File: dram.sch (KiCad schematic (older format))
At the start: 25 parts

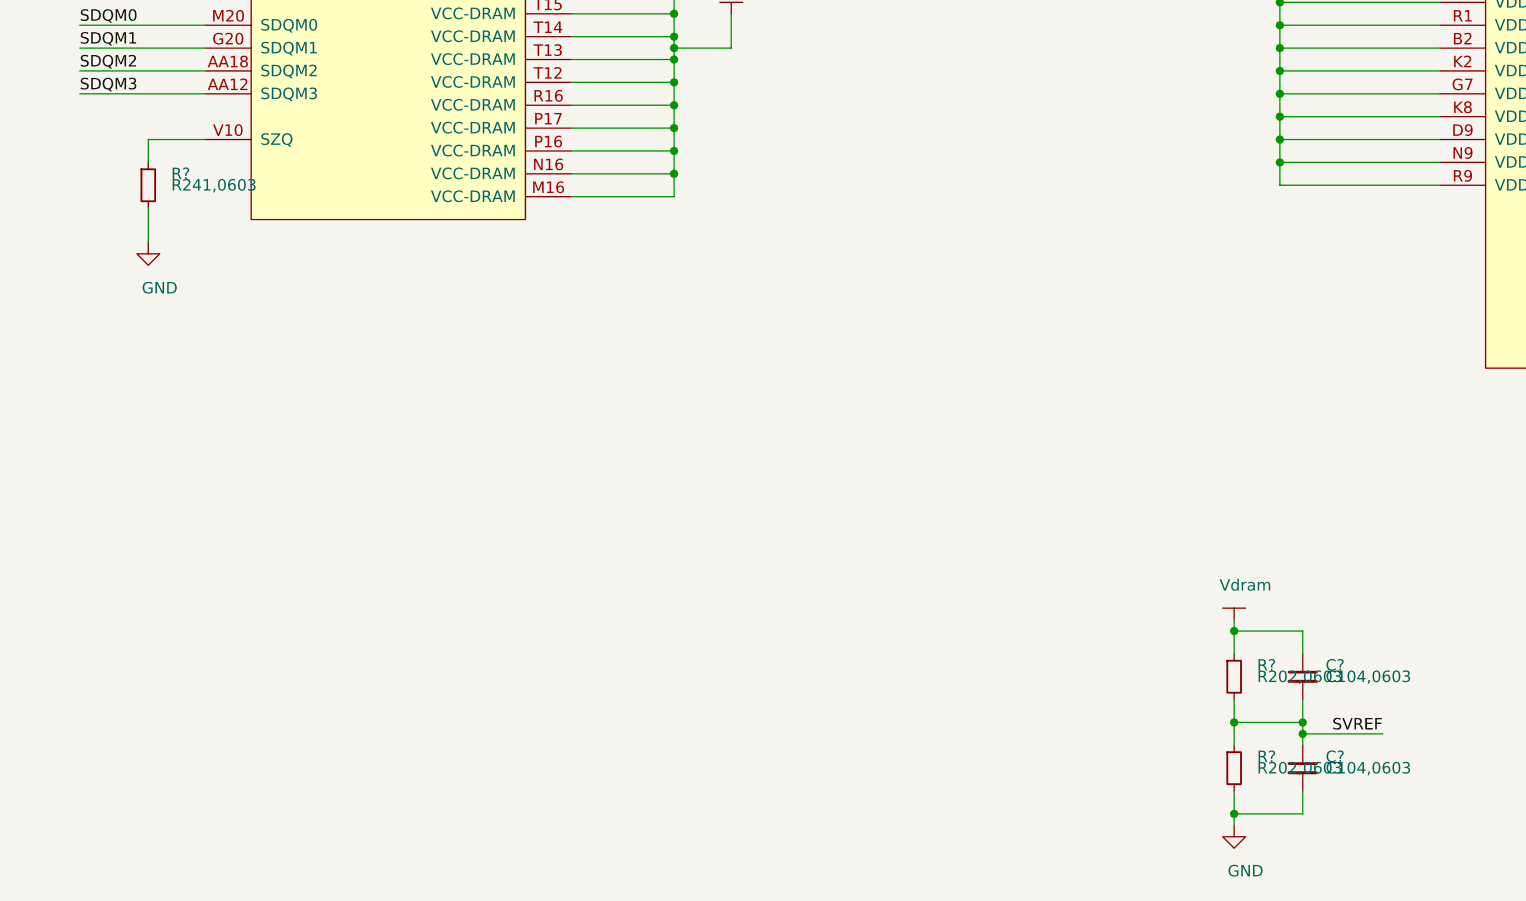
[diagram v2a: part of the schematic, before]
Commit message: update Vdram capacitor,
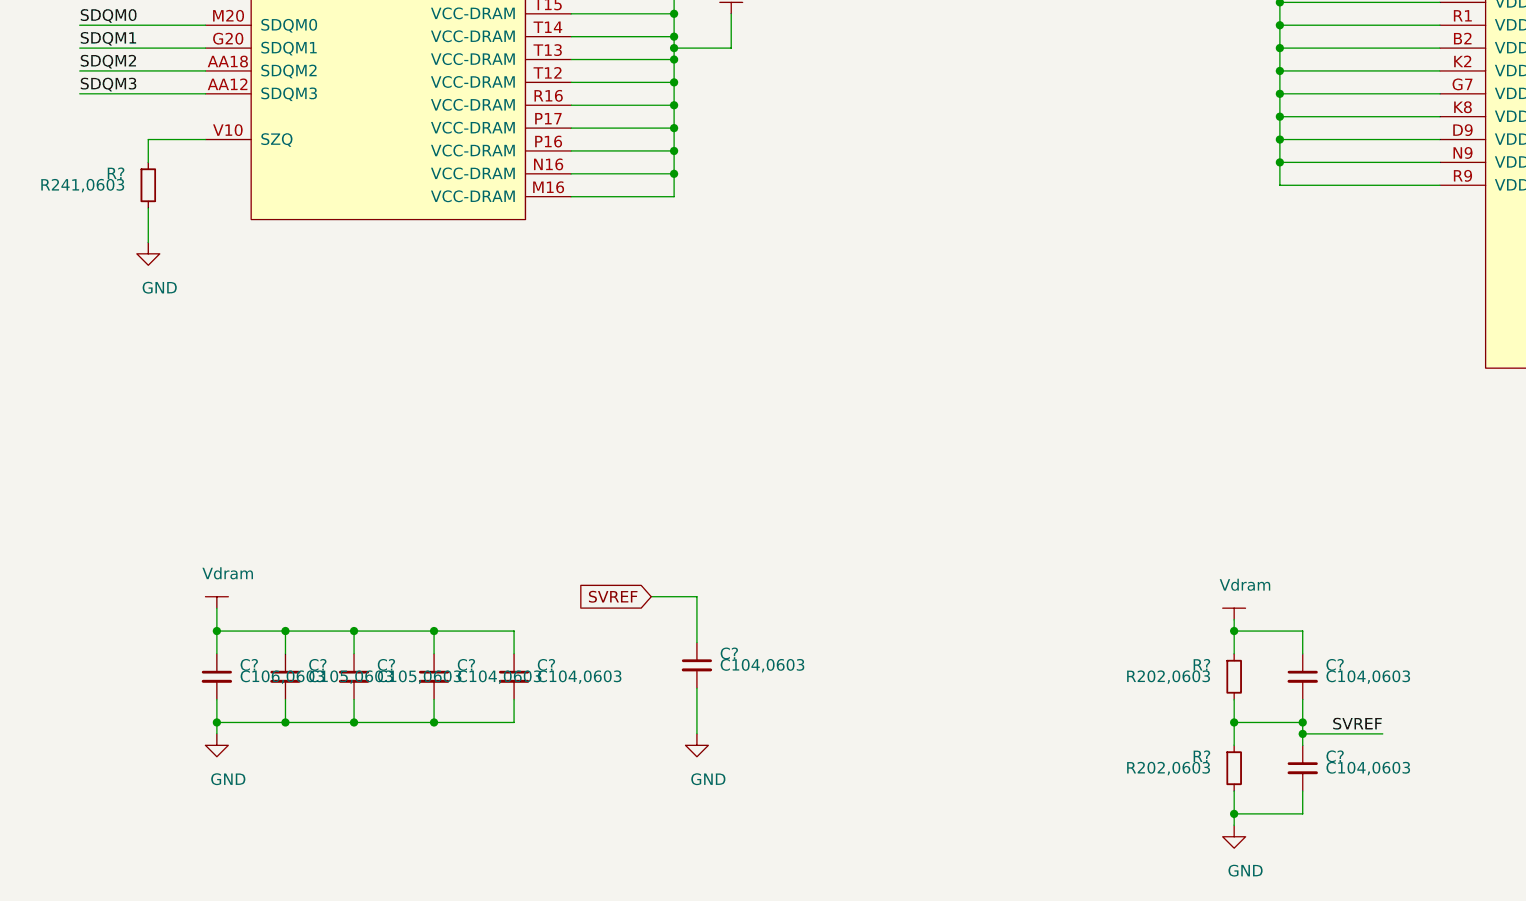
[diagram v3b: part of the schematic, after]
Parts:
- added C?: C106,0603, Capacitor_SMD:C_0603_1608Metric_Pad1.05x0.95mm_HandSolder, symbol taobao-c:C106,0603
- added C? (x2): C105,0603, Capacitor_SMD:C_0603_1608Metric_Pad1.05x0.95mm_HandSolder, symbol taobao-c:C105,0603
- added C? (x3): C104,0603, Capacitor_SMD:C_0603_1608Metric_Pad1.05x0.95mm_HandSolder, symbol taobao-c:C104,0603
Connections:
- net GND: now also C?.2, C?.2, C?.2, C?.2, C?.2, C?.2
- net SVREF: now also C?.1
- net Vdram: now also C?.1, C?.1, C?.1, C?.1, C?.1
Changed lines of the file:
@@
 AR Path="/5C5C55F2/5C2CA6EE" Ref="R?"  Part="1"
 AR Path="/5C273FE9/5C2CA6EE" Ref="R?"  Part="1"
-F 0 "R?" H 6950 9050 50  0000 L CNN
-F 1 "R202,0603" H 6950 9000 50  0000 L CNN
+F 0 "R?" H 6750 9050 50  0000 R CNN
+F 1 "R202,0603" H 6750 9000 50  0000 R CNN
 F 2 "Resistor_SMD:R_0603_1608Metric_Pad1.05x0.95mm_HandSolder" H 6850 9000 50  0001 C CNN
 F 3 "~" H 6850 9000 50  0001 C CNN
@@
 AR Path="/5C5C55F2/5C2CA73C" Ref="R?"  Part="1"
 AR Path="/5C273FE9/5C2CA73C" Ref="R?"  Part="1"
-F 0 "R?" H 6950 9450 50  0000 L CNN
-F 1 "R202,0603" H 6950 9400 50  0000 L CNN
+F 0 "R?" H 6750 9450 50  0000 R CNN
+F 1 "R202,0603" H 6750 9400 50  0000 R CNN
 F 2 "Resistor_SMD:R_0603_1608Metric_Pad1.05x0.95mm_HandSolder" H 6850 9400 50  0001 C CNN
 F 3 "~" H 6850 9400 50  0001 C CNN
@@
 U 1 1 5C5FA017
 P 2100 6850
-F 0 "R?" H 2200 6900 50  0000 L CNN
-F 1 "R241,0603" H 2200 6850 50  0000 L CNN
+F 0 "R?" H 2000 6900 50  0000 R CNN
+F 1 "R241,0603" H 2000 6850 50  0000 R CNN
 F 2 "Resistor_SMD:R_0603_1608Metric_Pad1.05x0.95mm_HandSolder" H 2100 6850 50  0001 C CNN
 F 3 "~" H 2100 6850 50  0001 C CNN
@@
 Wire Wire Line
 	1850 5050 2350 5050
+$Comp
+L taobao-components:Vdram #PWR?
+U 1 1 5C2AD72D
+P 2400 8700
+AR Path="/5C273FE9/5C786D7F/5C2AD72D" Ref="#PWR?"  Part="1"
+AR Path="/5C273FE9/5C7AC496/5C2AD72D" Ref="#PWR?"  Part="1"
+AR Path="/5C7B767A/5C786D7F/5C2AD72D" Ref="#PWR?"  Part="1"
+F 0 "#PWR?" H 2400 8550 50  0001 C CNN
+F 1 "Vdram" H 2450 8850 50  0000 C CNN
+F 2 "" H 2400 8700 50  0001 C CNN
+F 3 "" H 2400 8700 50  0001 C CNN
+	1    2400 8700
+	1    0    0    -1
+$EndComp
+$Comp
+L taobao-c:C106,0603 C?
+U 1 1 5C2AD733
+P 2400 9000
+AR Path="/5C273FE9/5C786D7F/5C2AD733" Ref="C?"  Part="1"
+AR Path="/5C273FE9/5C7AC496/5C2AD733" Ref="C?"  Part="1"
+AR Path="/5C7B767A/5C786D7F/5C2AD733" Ref="C?"  Part="1"
+F 0 "C?" H 2500 9050 50  0000 L CNN
+F 1 "C106,0603" H 2500 9000 50  0000 L CNN
+F 2 "Capacitor_SMD:C_0603_1608Metric_Pad1.05x0.95mm_HandSolder" H 2400 9000 50  0001 C CNN
+F 3 "~" H 2400 9000 50  0001 C CNN
+	1    2400 9000
+	1    0    0    -1
+$EndComp
+$Comp
+L power:GND #PWR?
+U 1 1 5C2AD73A
+P 2400 9250
+AR Path="/5C273FE9/5C786D7F/5C2AD73A" Ref="#PWR?"  Part="1"
+AR Path="/5C273FE9/5C7AC496/5C2AD73A" Ref="#PWR?"  Part="1"
+AR Path="/5C7B767A/5C786D7F/5C2AD73A" Ref="#PWR?"  Part="1"
+F 0 "#PWR?" H 2400 9000 50  0001 C CNN
+F 1 "GND" H 2450 9050 50  0000 C CNN
+F 2 "" H 2400 9250 50  0001 C CNN
+F 3 "" H 2400 9250 50  0001 C CNN
+	1    2400 9250
+	1    0    0    -1
+$EndComp
+Wire Wire Line
+	2400 9250 2400 9200
+Wire Wire Line
+	2400 8700 2400 8800
+$Comp
+L taobao-c:C105,0603 C?
+U 1 1 5C2AD742
+P 2700 9000
+AR Path="/5C273FE9/5C786D7F/5C2AD742" Ref="C?"  Part="1"
+AR Path="/5C273FE9/5C7AC496/5C2AD742" Ref="C?"  Part="1"
+AR Path="/5C7B767A/5C786D7F/5C2AD742" Ref="C?"  Part="1"
+F 0 "C?" H 2800 9050 50  0000 L CNN
+F 1 "C105,0603" H 2800 9000 50  0000 L CNN
+F 2 "Capacitor_SMD:C_0603_1608Metric_Pad1.05x0.95mm_HandSolder" H 2700 9000 50  0001 C CNN
+F 3 "~" H 2700 9000 50  0001 C CNN
+	1    2700 9000
+	1    0    0    -1
+$EndComp
+Wire Wire Line
+	2700 8900 2700 8800
+Wire Wire Line
+	2700 8800 2400 8800
+Connection ~ 2400 8800
+Wire Wire Line
+	2400 8800 2400 8900
+Wire Wire Line
+	2700 9100 2700 9200
+Wire Wire Line
+	2700 9200 2400 9200
+Connection ~ 2400 9200
+Wire Wire Line
+	2400 9200 2400 9100
+$Comp
+L taobao-c:C105,0603 C?
+U 1 1 5C2AD751
+P 3000 9000
+AR Path="/5C273FE9/5C786D7F/5C2AD751" Ref="C?"  Part="1"
+AR Path="/5C273FE9/5C7AC496/5C2AD751" Ref="C?"  Part="1"
+AR Path="/5C7B767A/5C786D7F/5C2AD751" Ref="C?"  Part="1"
+F 0 "C?" H 3100 9050 50  0000 L CNN
+F 1 "C105,0603" H 3100 9000 50  0000 L CNN
+F 2 "Capacitor_SMD:C_0603_1608Metric_Pad1.05x0.95mm_HandSolder" H 3000 9000 50  0001 C CNN
+F 3 "~" H 3000 9000 50  0001 C CNN
+	1    3000 9000
+	1    0    0    -1
+$EndComp
+Wire Wire Line
+	3000 8900 3000 8800
+Wire Wire Line
+	3000 8800 2700 8800
+Wire Wire Line
+	3000 9100 3000 9200
+Wire Wire Line
+	3000 9200 2700 9200
+Connection ~ 2700 8800
+Connection ~ 2700 9200
+$Comp
+L taobao-c:C104,0603 C?
+U 1 1 5C2AD75E
+P 3350 9000
+AR Path="/5C273FE9/5C786D7F/5C2AD75E" Ref="C?"  Part="1"
+AR Path="/5C273FE9/5C7AC496/5C2AD75E" Ref="C?"  Part="1"
+AR Path="/5C7B767A/5C786D7F/5C2AD75E" Ref="C?"  Part="1"
+F 0 "C?" H 3450 9050 50  0000 L CNN
+F 1 "C104,0603" H 3450 9000 50  0000 L CNN
+F 2 "Capacitor_SMD:C_0603_1608Metric_Pad1.05x0.95mm_HandSolder" H 3350 9000 50  0001 C CNN
+F 3 "~" H 3350 9000 50  0001 C CNN
+	1    3350 9000
+	1    0    0    -1
+$EndComp
+Wire Wire Line
+	3350 8900 3350 8800
+Wire Wire Line
+	3350 8800 3000 8800
+Connection ~ 3000 8800
+Wire Wire Line
+	3350 9100 3350 9200
+Wire Wire Line
+	3350 9200 3000 9200
+Connection ~ 3000 9200
+$Comp
+L taobao-c:C104,0603 C?
+U 1 1 5C2AD76B
+P 3700 9000
+AR Path="/5C273FE9/5C786D7F/5C2AD76B" Ref="C?"  Part="1"
+AR Path="/5C273FE9/5C7AC496/5C2AD76B" Ref="C?"  Part="1"
+AR Path="/5C7B767A/5C786D7F/5C2AD76B" Ref="C?"  Part="1"
+F 0 "C?" H 3800 9050 50  0000 L CNN
+F 1 "C104,0603" H 3800 9000 50  0000 L CNN
+F 2 "Capacitor_SMD:C_0603_1608Metric_Pad1.05x0.95mm_HandSolder" H 3700 9000 50  0001 C CNN
+F 3 "~" H 3700 9000 50  0001 C CNN
+	1    3700 9000
+	1    0    0    -1
+$EndComp
+Wire Wire Line
+	3700 8900 3700 8800
+Wire Wire Line
+	3700 8800 3350 8800
+Wire Wire Line
+	3700 9100 3700 9200
+Wire Wire Line
+	3700 9200 3350 9200
+Connection ~ 3350 8800
+Connection ~ 3350 9200
+Text GLabel 4300 8650 0    50   Input ~ 0
+SVREF
+$Comp
+L taobao-c:C104,0603 C?
+U 1 1 5C2AD779
+P 4500 8950
+AR Path="/5C273FE9/5C786D7F/5C2AD779" Ref="C?"  Part="1"
+AR Path="/5C273FE9/5C7AC496/5C2AD779" Ref="C?"  Part="1"
+AR Path="/5C7B767A/5C786D7F/5C2AD779" Ref="C?"  Part="1"
+F 0 "C?" H 4600 9000 50  0000 L CNN
+F 1 "C104,0603" H 4600 8950 50  0000 L CNN
+F 2 "Capacitor_SMD:C_0603_1608Metric_Pad1.05x0.95mm_HandSolder" H 4500 8950 50  0001 C CNN
+F 3 "~" H 4500 8950 50  0001 C CNN
+	1    4500 8950
+	1    0    0    -1
+$EndComp
+Wire Wire Line
+	4300 8650 4500 8650
+Wire Wire Line
+	4500 8650 4500 8850
+$Comp
+L power:GND #PWR?
+U 1 1 5C2AD782
+P 4500 9250
+AR Path="/5C273FE9/5C786D7F/5C2AD782" Ref="#PWR?"  Part="1"
+AR Path="/5C273FE9/5C7AC496/5C2AD782" Ref="#PWR?"  Part="1"
+AR Path="/5C7B767A/5C786D7F/5C2AD782" Ref="#PWR?"  Part="1"
+F 0 "#PWR?" H 4500 9000 50  0001 C CNN
+F 1 "GND" H 4550 9050 50  0000 C CNN
+F 2 "" H 4500 9250 50  0001 C CNN
+F 3 "" H 4500 9250 50  0001 C CNN
+	1    4500 9250
+	1    0    0    -1
+$EndComp
+Wire Wire Line
+	4500 9250 4500 9050
 $EndSCHEMATC
